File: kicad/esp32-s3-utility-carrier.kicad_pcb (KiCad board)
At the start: 2 copper layers, 130 x 85 mm, 31 parts, among them SW1 BTN1, SW2 BTN2, SW3 BTN3, U2 SN74AHCT125N

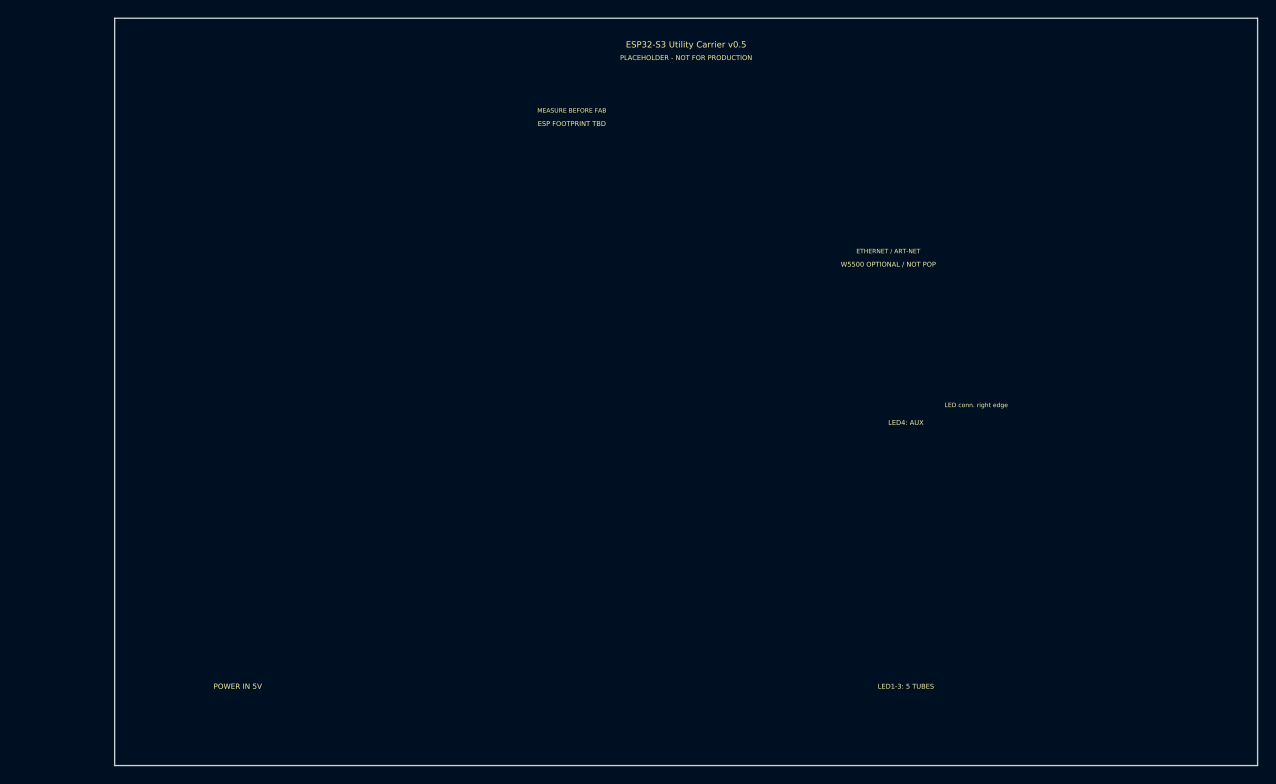
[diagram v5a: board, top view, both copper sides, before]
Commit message: fix(pcb): align placement with zone layout
Reorganize 130×85 mm placeholder PCB into six functional zones per layout
diagram; airwires only, no pours or placeholder tracks.

Co-authored-by: Cursor <cursoragent@cursor.com>
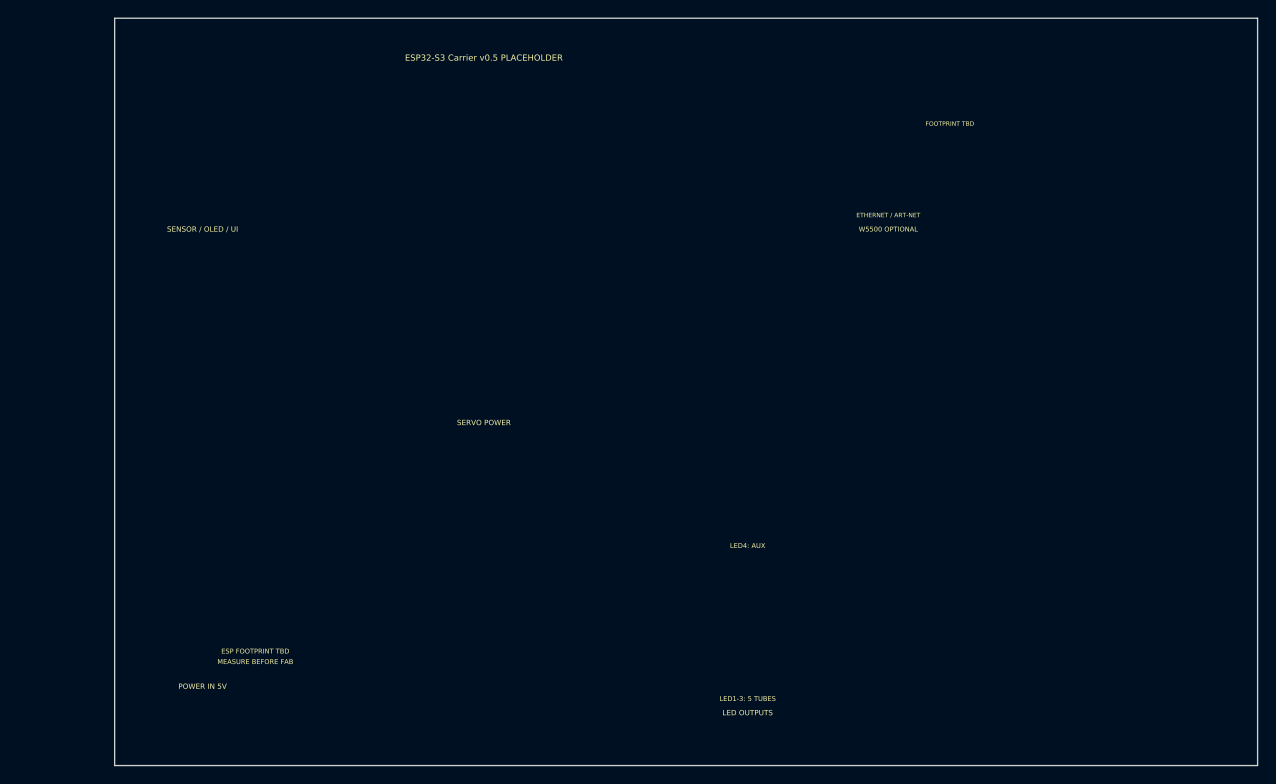
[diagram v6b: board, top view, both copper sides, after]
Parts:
- moved SW1 50.0 mm to (62.0, 10.0)
- moved SW2 50.0 mm to (72.0, 10.0)
- moved SW3 50.0 mm to (82.0, 10.0)
- moved J_BTN 41.2 mm to (50.0, 10.0)
- moved F_ESP 36.5 mm to (16.0, 20.0)
- moved C_SERVO 34.4 mm to (52.0, 30.0)
- moved SJ_SERVO 34.4 mm to (42.0, 30.0)
- moved J_SERVO2 31.6 mm to (55.0, 38.0)
- moved J_SERVO1 28.6 mm to (42.0, 38.0)
- moved U2 26.1 mm to (62.0, 58.0)
- moved R_LED4 24.2 mm to (84.0, 58.0)
- moved C_AHCT 24.1 mm to (72.0, 50.0)
- moved R_LED3 23.4 mm to (84.0, 64.0)
- moved R_LED2 22.8 mm to (84.0, 70.0)
- moved R_LED1 22.4 mm to (84.0, 76.0)
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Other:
- board text added: "ANT"
- board text added: "ESP32-S3 Carrier v0.5 PLACEHOLDER"
- board text added: "FOOTPRINT TBD"
- board text added: "LED OUTPUTS"
- board text added: "SENSOR / OLED / UI"
- board text added: "SERVO POWER"
- board text added: "USB"
- board text added: "W5500 OPTIONAL"
- board text removed: "1 POWER"
- board text removed: "2 ESP32-S3 DEVKIT"
- board text removed: "3 LED OUTPUTS"
- board text removed: "4 SENSOR / OLED / UI"
- board text removed: "5 SERVO POWER"
- board text removed: "6 W5500 / ETHERNET"
- board text removed: "ANT keep-out"
- board text removed: "ESP32-S3 Utility Carrier v0.5"
- board text removed: "LED conn. right edge"
- board text removed: "PLACEHOLDER - NOT FOR PRODUCTION"
- board text removed: "USB edge"
- board text removed: "W5500 OPTIONAL / NOT POP"

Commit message: fix(pcb): place components by explicit coordinates
v0.6: PCB_PLACE/PCB_SILK drive 130×85 mm layout with overlap checks;
F_ESP x=45 for J_I2C clearance; silk nudges documented in layout plan.

Co-authored-by: Cursor <cursoragent@cursor.com>
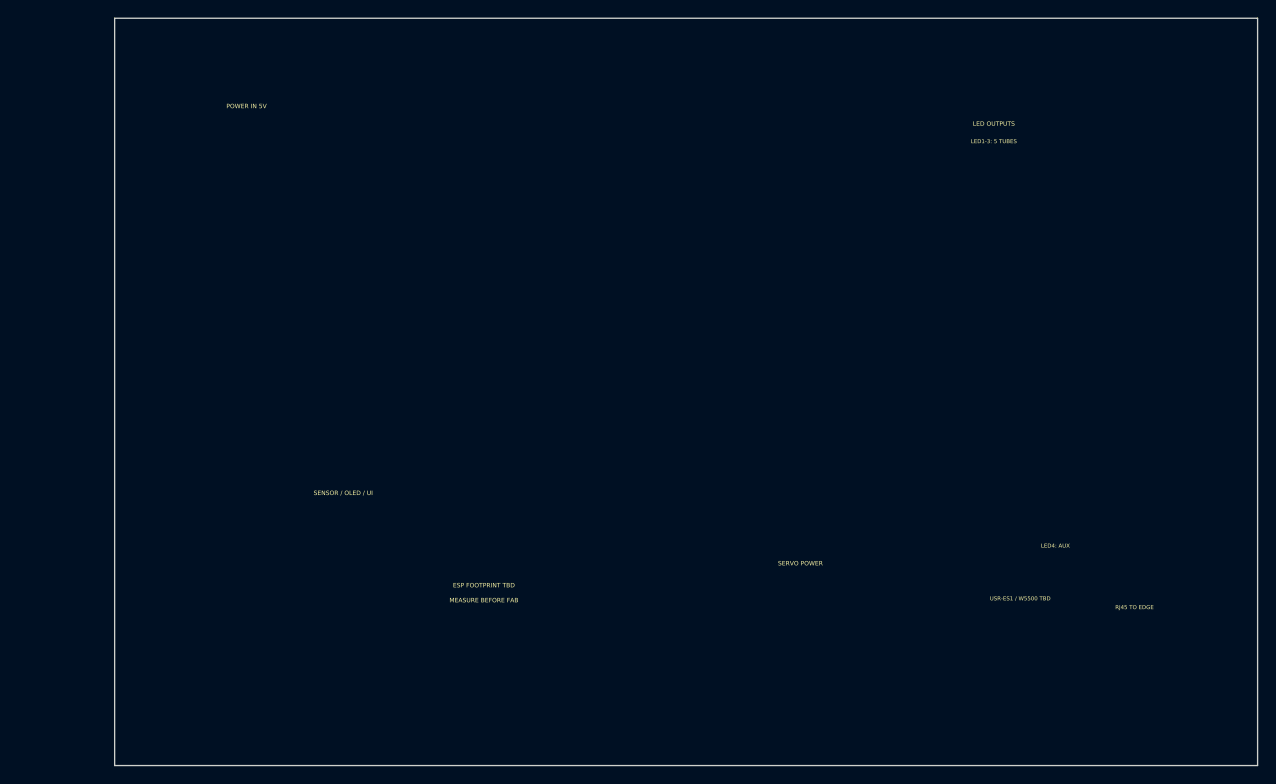
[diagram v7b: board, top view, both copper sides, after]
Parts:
- removed F_OLED: OLED_DIR, Connector_PinHeader_2.54mm:PinHeader_1x04_P2.54mm_Vertical
- moved J_BTN 71.6 mm to (8.00, 68.0)
- moved SW1 69.3 mm to (24.0, 68.0)
- moved SW2 69.3 mm to (34.0, 68.0)
- moved SW3 69.3 mm to (44.0, 68.0)
- moved R_LED1 58.9 mm to (94.0, 18.0)
- moved J_LED1 58.1 mm to (112.0, 18.0)
- moved J_W5500 58.0 mm to (94.0, 70.0)
- moved C_MAIN 54.0 mm to (22.0, 14.0)
- moved J_MAIN 54.0 mm to (8.00, 14.0)
- moved J_ENC 52.3 mm to (56.0, 68.0)
- moved J_LD2450 48.0 mm to (8.00, 58.0)
- moved J_I2C 48.0 mm to (36.0, 58.0)
- moved J_OLED_EXT 48.0 mm to (22.0, 58.0)
- moved J_SERVO2 46.2 mm to (84.0, 74.0)
- moved J_SERVO1 45.6 mm to (70.0, 74.0)
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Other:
- board text added: "RJ45 TO EDGE"
- board text added: "USR-ES1 / W5500 TBD"
- board text removed: "ANT"
- board text removed: "ESP32-S3 Carrier v0.5 PLACEHOLDER"
- board text removed: "ETHERNET / ART-NET"
- board text removed: "FOOTPRINT TBD"
- board text removed: "USB"
- board text removed: "W5500 OPTIONAL"

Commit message: fix(pcb): align placement plan and add visible routing
v0.7: approved zone layout in PCB_PLACE, partial F.Cu routing for
LED/servo/main power, W5500 5 mm margin, overlap-checked silk.

Co-authored-by: Cursor <cursoragent@cursor.com>
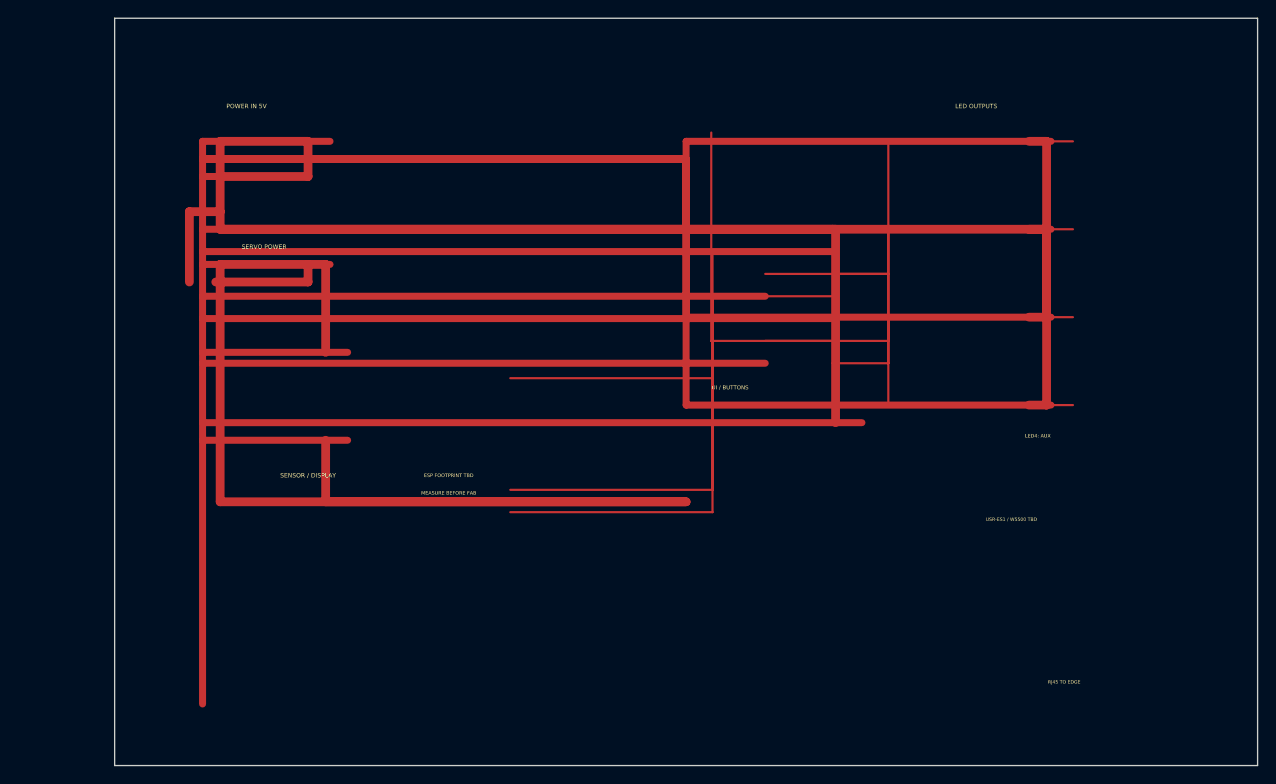
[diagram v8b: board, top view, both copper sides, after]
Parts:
- moved C_SERVO 70.0 mm to (22.0, 28.0)
- moved J_SERVO2 70.0 mm to (24.0, 38.0)
- moved SJ_SERVO 70.0 mm to (10.0, 30.0)
- moved J_BTN 65.1 mm to (70.0, 48.0)
- moved SW1 55.5 mm to (78.0, 55.0)
- moved SW2 53.6 mm to (86.0, 55.0)
- moved J_SERVO1 52.8 mm to (24.0, 48.0)
- moved SW3 51.7 mm to (94.0, 55.0)
- moved J_ENC 24.5 mm to (80.0, 63.0)
- moved J_LED4 12.8 mm to (104.0, 44.0)
- moved R_LED4 11.7 mm to (88.0, 44.0)
- moved J_LED3 11.3 mm to (104.0, 34.0)
- moved J_LED2 10.0 mm to (104.0, 24.0)
- moved R_LED3 10.0 mm to (88.0, 34.0)
- moved J_LED1 8.94 mm to (104.0, 14.0)
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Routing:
- net GND: track 0.00 -> 984.2 mm
- net 5V_SERVO: track 0.00 -> 162.5 mm
- net 5V_LED: track 0.00 -> 142.0 mm
- net 5V_LOGIC: track 0.00 -> 94.0 mm
- net LED1_IN: track 0.00 -> 58.6 mm
- net LED1_DATA: track 0.00 -> 50.1 mm
- net LED2_IN: track 0.00 -> 48.5 mm
- net LED2_DATA: track 0.00 -> 47.7 mm
- net LED4_IN: track 0.00 -> 45.9 mm
- net 5V_MAIN: track 0.00 -> 43.5 mm
- net LED4_DATA: track 0.00 -> 42.3 mm
- net LED3_IN: track 0.00 -> 37.5 mm
- net LED3_DATA: track 0.00 -> 32.6 mm
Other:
- board text added: "SENSOR / DISPLAY"
- board text added: "UI / BUTTONS"
- board text removed: "LED1-3: 5 TUBES"
- board text removed: "SENSOR / OLED / UI"
